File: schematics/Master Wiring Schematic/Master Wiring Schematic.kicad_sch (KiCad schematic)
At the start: 0 parts

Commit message: Work
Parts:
- added BT1: Elecstor_12.8V_24Ah, symbol Device:Battery
- added F1: 40A_MIDI_Fuse, symbol Device:Fuse
- added J1: M5_Ring_Terminals, symbol Connector_Generic:Conn_01x02
- added J2: Raspberry_Pi_4, symbol Connector:Raspberry_Pi_4
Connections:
- new net: BT1.1 (+), F1.1, J1.1 (Pin_1)
- new net: J2.1 (3V3), J2.17 (3V3)
- new net: J2.14 (GND), J2.20 (GND), J2.25 (GND), J2.30 (GND), J2.34 (GND), J2.39 (GND), J2.6 (GND), J2.9 (GND)
- new net: J2.2 (5V), J2.4 (5V)
- new net +12.8V_VBAT: F1.2
- new net GND: BT1.2 (-), J1.2 (Pin_2)
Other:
- note added: "Battery Circuitry"

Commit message: Placing MCU on sheet
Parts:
- added A1: Arduino_Mega2560_R3_Shield, PCM_arduino-library:Arduino_Mega2560_R3_Shield, symbol arduino-library:Arduino_Mega2560_R3_Shield
- added J3: UBEC_5V_3A, symbol Connector_Generic:Conn_01x04

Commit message: Powering the Brains of the Rover
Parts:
- removed J3: UBEC_5V_3A, symbol Connector_Generic:Conn_01x04
- added F2: 5A_Inline_Fuse, symbol Device:Fuse
- added PS1: UBEC_5V_3A, Converter_DCDC:Converter_DCDC_XP_POWER-ITXxxxxSA_THT, symbol Converter_DCDC:ITX1209SA
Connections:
- net +12.8V_VBAT: now also F2.1
- net GND: now also PS1.1 (-Vin), PS1.7 (-Vout)
- net +5V: now reaches A1.5V1 (5V)
- net +5V: now also A1.5V3 (5V), A1.5V4 (5V), J2.2 (5V), J2.4 (5V), PS1.6 (+Vout)
- new net: F2.2, PS1.2 (+Vin)
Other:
- company: (none) -> UCT Space and Astronomy Society
- title: (none) -> Cars4Mars Master Schematic
- moved on the sheet: A1, J2

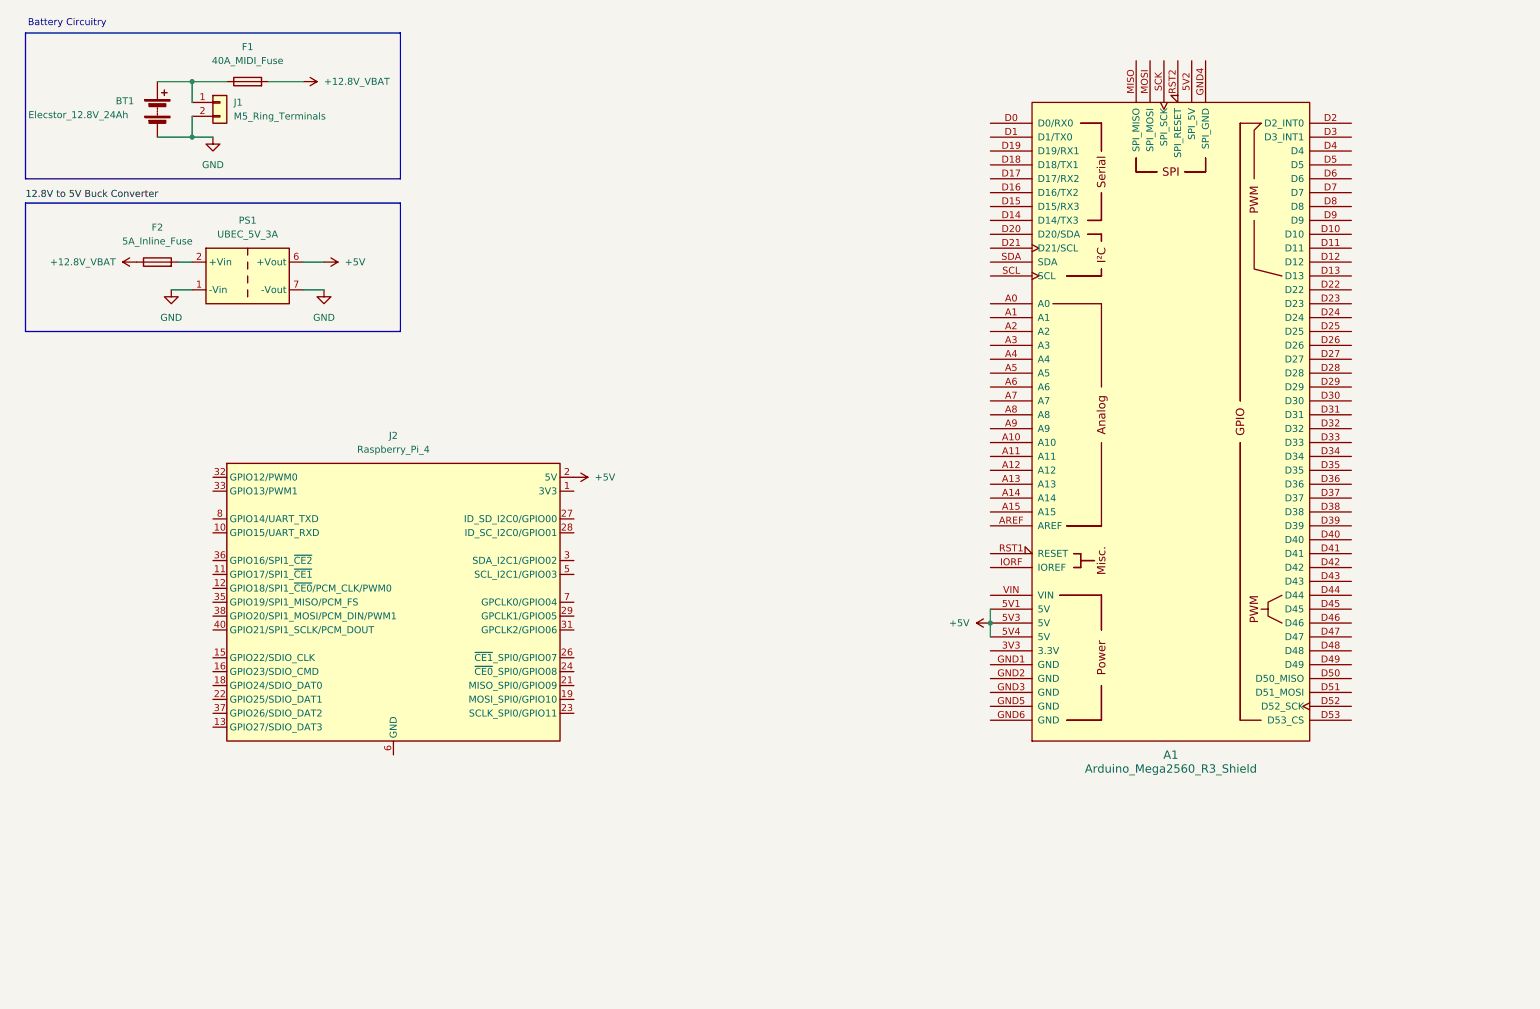
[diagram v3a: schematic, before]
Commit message: Power and Data Link between Pi and Arduino
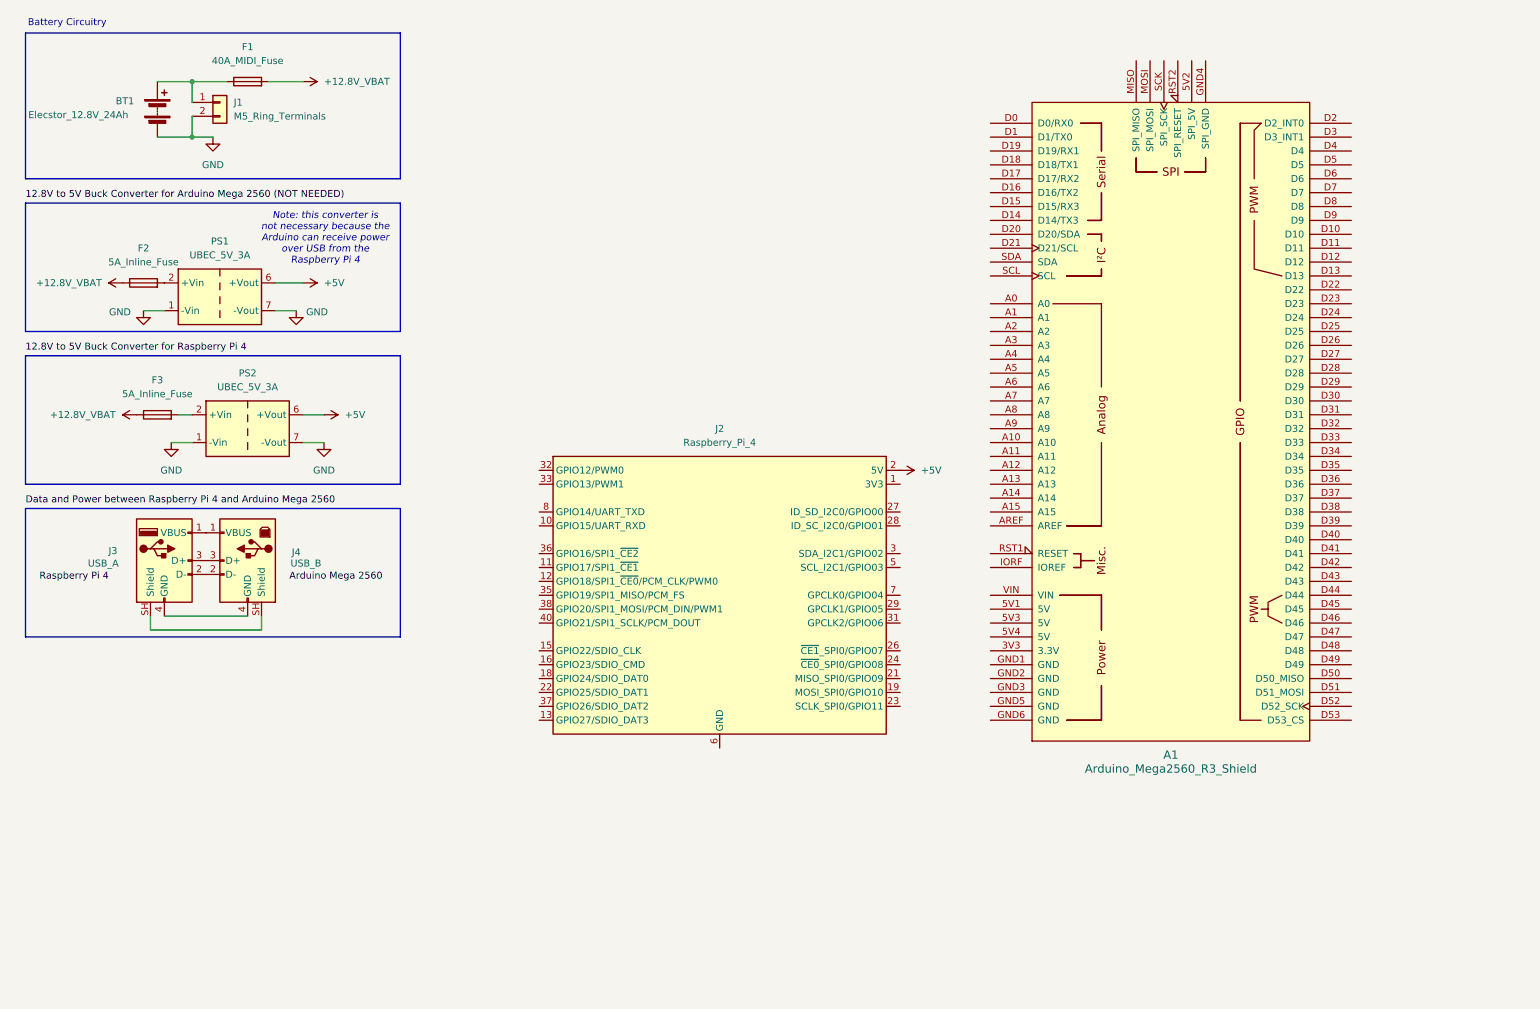
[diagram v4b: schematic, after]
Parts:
- added F3: 5A_Inline_Fuse, symbol Device:Fuse
- added J3: USB_A, symbol Connector:USB_A
- added J4: USB_B, symbol Connector:USB_B
- added PS2: UBEC_5V_3A, Converter_DCDC:Converter_DCDC_XP_POWER-ITXxxxxSA_THT, symbol Converter_DCDC:ITX1209SA
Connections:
- net +12.8V_VBAT: now also F3.1
- net +5V: now also PS2.6 (+Vout); no longer A1.5V1 (5V), A1.5V3 (5V), A1.5V4 (5V)
- net GND: now also PS2.1 (-Vin), PS2.7 (-Vout)
- new net: J3.1 (VBUS), J4.1 (VBUS)
- new net: J3.2 (D-), J4.2 (D-)
- new net: J3.3 (D+), J4.3 (D+)
- new net: J3.4 (GND), J4.4 (GND)
- new net: J3.SH (Shield), J4.SH (Shield)
- new net: F3.2, PS2.2 (+Vin)
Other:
- note added: "Note: this converter is not necessary because the Arduino can receive power over USB from the Raspberry Pi 4"
- moved on the sheet: F2, J2, PS1

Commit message: Drive system components are being laid out on a subsheet
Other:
- added sheet Drive System (drive_system_wiring.kicad_sch)
- moved on the sheet: J2
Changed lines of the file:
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@@
 	(symbol
 		(lib_id "power:+5V")
-		(at 175.26 97.79 270)
+		(at 160.02 133.35 270)
 		(unit 1)
 		(body_style 1)
@@
 		(fields_autoplaced yes)
 		(property "Reference" "#PWR07"
-			(at 171.45 97.79 0)
+			(at 156.21 133.35 0)
 			(hide yes)
 			(show_name no)
@@
 		)
 		(property "Value" "+5V"
-			(at 179.07 97.7899 90)
+			(at 163.83 133.3499 90)
 			(show_name no)
 			(do_not_autoplace no)
@@
 		)
 		(property "Footprint" ""
-			(at 175.26 97.79 0)
+			(at 160.02 133.35 0)
 			(hide yes)
 			(show_name no)
@@
 		)
 		(property "Datasheet" ""
-			(at 175.26 97.79 0)
+			(at 160.02 133.35 0)
 			(hide yes)
 			(show_name no)
@@
 		)
 		(property "Description" "Power symbol creates a global label with name \"+5V\""
-			(at 175.26 97.79 0)
+			(at 160.02 133.35 0)
 			(hide yes)
 			(show_name no)
@@
 	(symbol
 		(lib_id "Connector:Raspberry_Pi_4")
-		(at 142.24 120.65 0)
+		(at 127 156.21 0)
 		(unit 1)
 		(body_style 1)
@@
 		(fields_autoplaced yes)
 		(property "Reference" "J2"
-			(at 142.24 90.17 0)
+			(at 127 125.73 0)
 			(show_name no)
 			(do_not_autoplace no)
@@
 		)
 		(property "Value" "Raspberry_Pi_4"
-			(at 142.24 92.71 0)
+			(at 127 128.27 0)
 			(show_name no)
 			(do_not_autoplace no)
@@
 		)
 		(property "Footprint" ""
-			(at 212.344 168.148 0)
+			(at 197.104 203.708 0)
 			(hide yes)
 			(show_name no)
@@
 		)
 		(property "Datasheet" "https://datasheets.raspberrypi.com/rpi4/raspberry-pi-4-datasheet.pdf"
-			(at 157.988 152.908 0)
+			(at 142.748 188.468 0)
 			(hide yes)
 			(show_name no)
@@
 		)
 		(property "Description" "Raspberry Pi 4 Model B"
-			(at 157.988 150.368 0)
+			(at 142.748 185.928 0)
 			(hide yes)
 			(show_name no)
@@
 		)
 	)
+	(sheet
+		(at 120.65 76.835)
+		(size 30.48 15.875)
+		(exclude_from_sim no)
+		(in_bom yes)
+		(on_board yes)
+		(dnp no)
+		(fields_autoplaced yes)
+		(stroke
+			(width 0.1524)
+			(type solid)
+		)
+		(fill
+			(color 0 0 0 0)
+		)
+		(property "Sheetname" "Drive System"
+			(at 120.65 76.1234 0)
+			(show_name no)
+			(do_not_autoplace no)
+			(effects
+				(font
+					(size 1.27 1.27)
+				)
+				(justify left bottom)
+			)
+		)
+		(property "Sheetfile" "drive_system_wiring.kicad_sch"
+			(at 120.65 93.2946 0)
+			(show_name no)
+			(do_not_autoplace no)
+			(effects
+				(font
+					(size 1.27 1.27)
+				)
+				(justify left top)
+			)
+		)
+		(instances
+			(project "Master Wiring Schematic"
+				(path "/2e4b1b4a-890e-4898-88a8-3fbb3ecae80d"
+					(page "2")
+				)
+			)
+		)
+	)

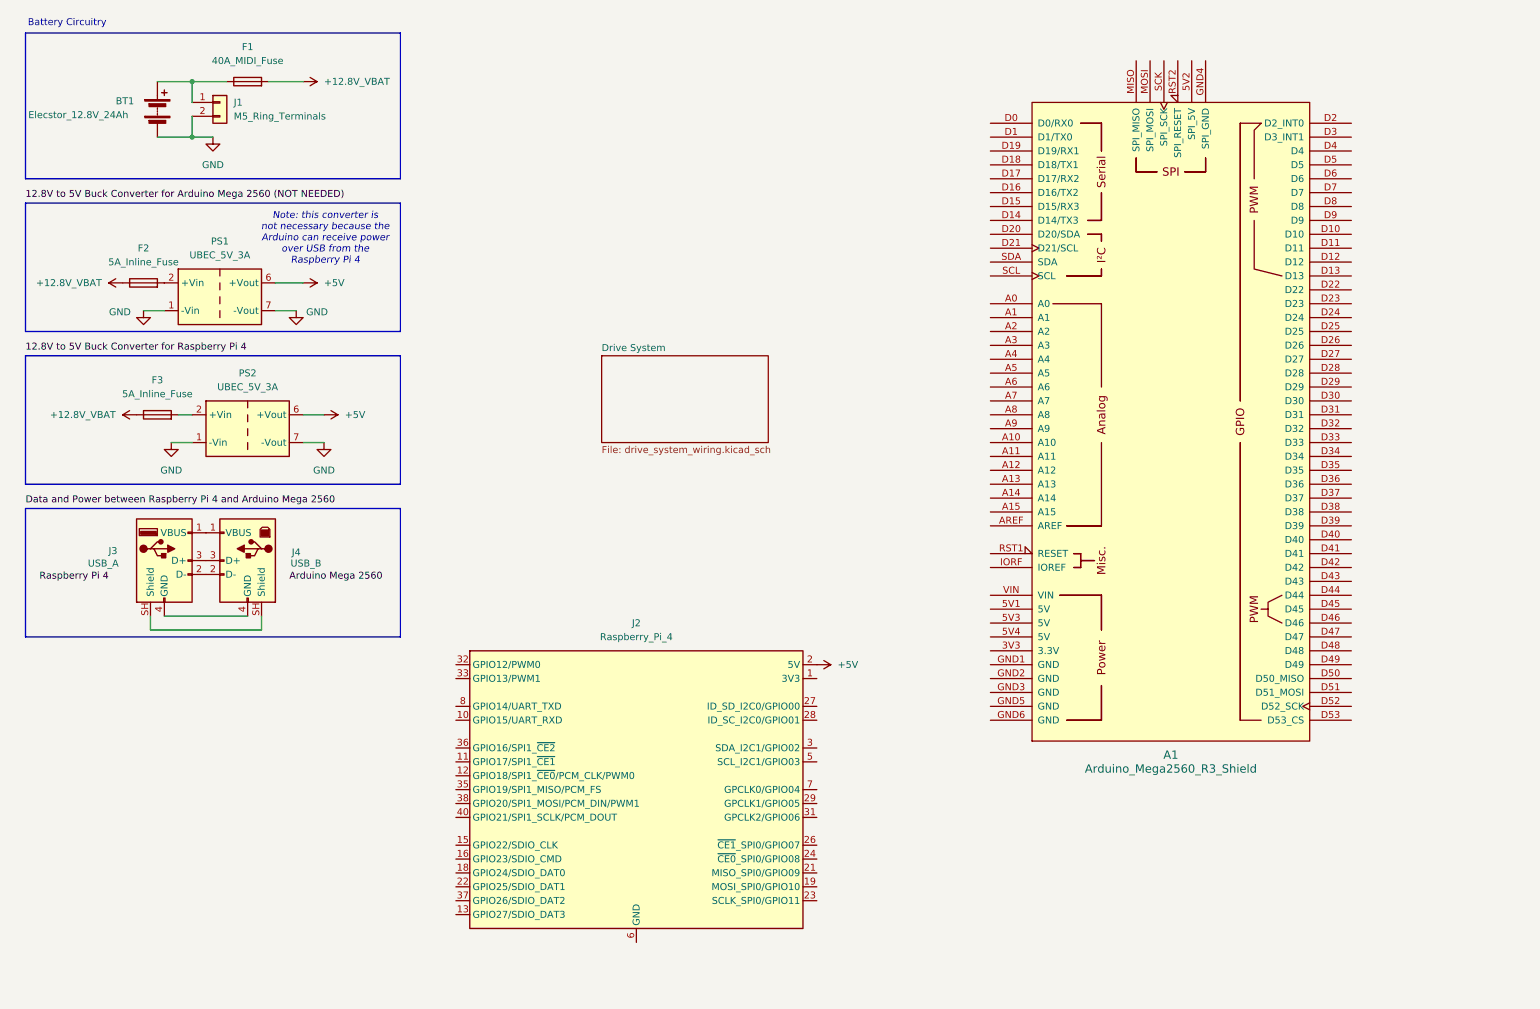
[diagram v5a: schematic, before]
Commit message: Drive system components are being laid out on a subsheet
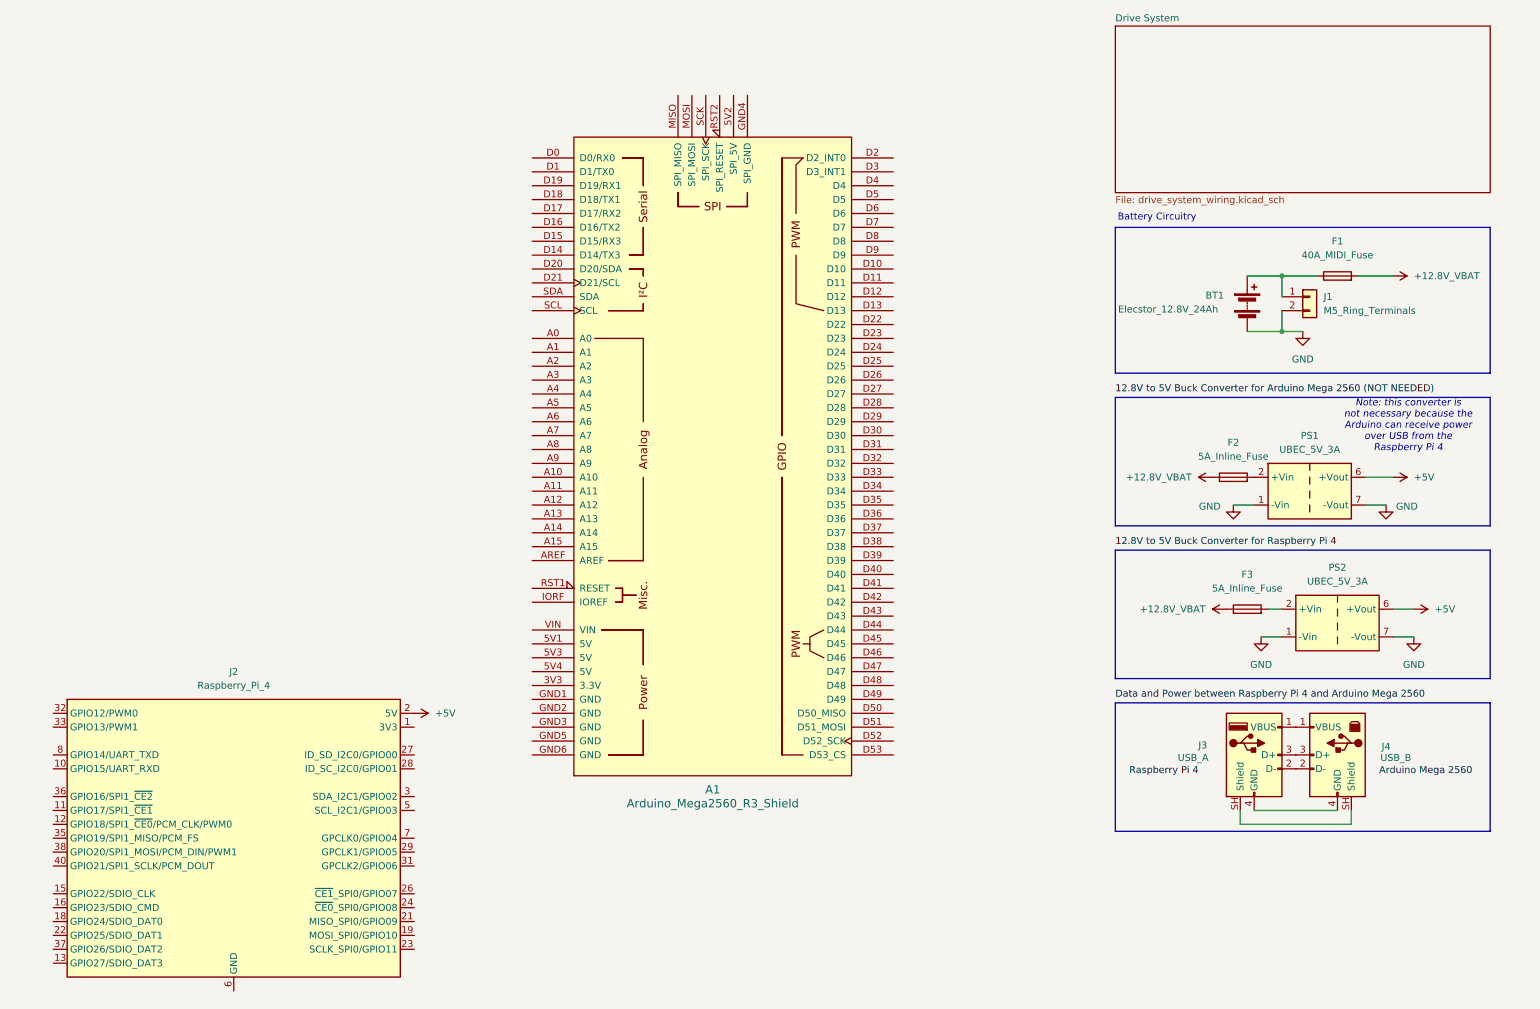
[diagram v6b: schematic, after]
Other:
- moved on the sheet: A1, BT1, F1, F2, F3, J1, J2, J3, J4, PS1, PS2

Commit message: Drive system components are being laid out on a subsheet
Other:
- moved on the sheet: A1, J2
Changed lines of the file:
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@@
 		)
 	)
-	(text "Note: this converter is \nnot necessary because the \nArduino can receive power \nover USB from the \nRaspberry Pi 4"
-		(exclude_from_sim no)
-		(at 268.224 89.662 0)
+	(text "Note: this converter is \nnot necessary because the \nArduino can receive power \nover USB from the \nRaspberry Pi 4 "
+		(exclude_from_sim no)
+		(at 282.956 90.932 0)
 		(effects
 			(font
@@
 				(italic yes)
 			)
+			(justify right)
 		)
 	)
@@
 		(pts
 			(xy 245.11 72.39) (xy 248.92 72.39)
+		)
+		(stroke
+			(width 0)
+			(type default)
+		)
+	)
+	(wire
+		(pts
+			(xy 90.17 123.19) (xy 86.36 142.24)
 		)
 		(stroke
@@
 	(symbol
 		(lib_id "arduino-library:Arduino_Mega2560_R3_Shield")
-		(at 140.97 95.25 0)
+		(at 156.21 90.17 0)
 		(unit 1)
 		(body_style 1)
@@
 		(fields_autoplaced yes)
 		(property "Reference" "A1"
-			(at 140.97 156.21 0)
+			(at 156.21 151.13 0)
 			(show_name no)
 			(do_not_autoplace no)
@@
 		)
 		(property "Value" "Arduino_Mega2560_R3_Shield"
-			(at 140.97 158.75 0)
+			(at 156.21 153.67 0)
 			(show_name no)
 			(do_not_autoplace no)
@@
 		)
 		(property "Footprint" "PCM_arduino-library:Arduino_Mega2560_R3_Shield"
-			(at 140.97 168.91 0)
+			(at 156.21 163.83 0)
 			(hide yes)
 			(show_name no)
@@
 		)
 		(property "Datasheet" "https://docs.arduino.cc/hardware/mega-2560"
-			(at 140.97 165.1 0)
+			(at 156.21 160.02 0)
 			(hide yes)
 			(show_name no)
@@
 		)
 		(property "Description" "Shield for Arduino Mega 2560 R3"
-			(at 140.97 95.25 0)
+			(at 156.21 90.17 0)
 			(hide yes)
 			(show_name no)
@@
 	(symbol
 		(lib_id "Connector:Raspberry_Pi_4")
-		(at 53.34 165.1 0)
+		(at 57.15 146.05 0)
 		(unit 1)
 		(body_style 1)
@@
 		(fields_autoplaced yes)
 		(property "Reference" "J2"
-			(at 53.34 134.62 0)
+			(at 57.15 115.57 0)
 			(show_name no)
 			(do_not_autoplace no)
@@
 		)
 		(property "Value" "Raspberry_Pi_4"
-			(at 53.34 137.16 0)
+			(at 57.15 118.11 0)
 			(show_name no)
 			(do_not_autoplace no)
@@
 		)
 		(property "Footprint" ""
-			(at 123.444 212.598 0)
+			(at 127.254 193.548 0)
 			(hide yes)
 			(show_name no)
@@
 		)
 		(property "Datasheet" "https://datasheets.raspberrypi.com/rpi4/raspberry-pi-4-datasheet.pdf"
-			(at 69.088 197.358 0)
+			(at 72.898 178.308 0)
 			(hide yes)
 			(show_name no)
@@
 		)
 		(property "Description" "Raspberry Pi 4 Model B"
-			(at 69.088 194.818 0)
-			(hide yes)
-			(show_name no)
+			(at 72.898 175.768 0)
+			(hide yes)
+			(show_name no)
